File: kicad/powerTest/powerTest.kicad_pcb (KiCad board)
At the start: 2 copper layers, 34 x 30 mm, 40 parts, among them J1 Solar Panel, J10 Conn_01x01_Pin, J11 Conn_01x01_Pin, J2 BATT, J3 3V3 Sensor Bus, J4 Conn_01x01_Pin, J5 Conn_01x01_Pin, J6 Conn_01x01_Pin, J7 Conn_01x01_Pin, J8 Conn_01x01_Pin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

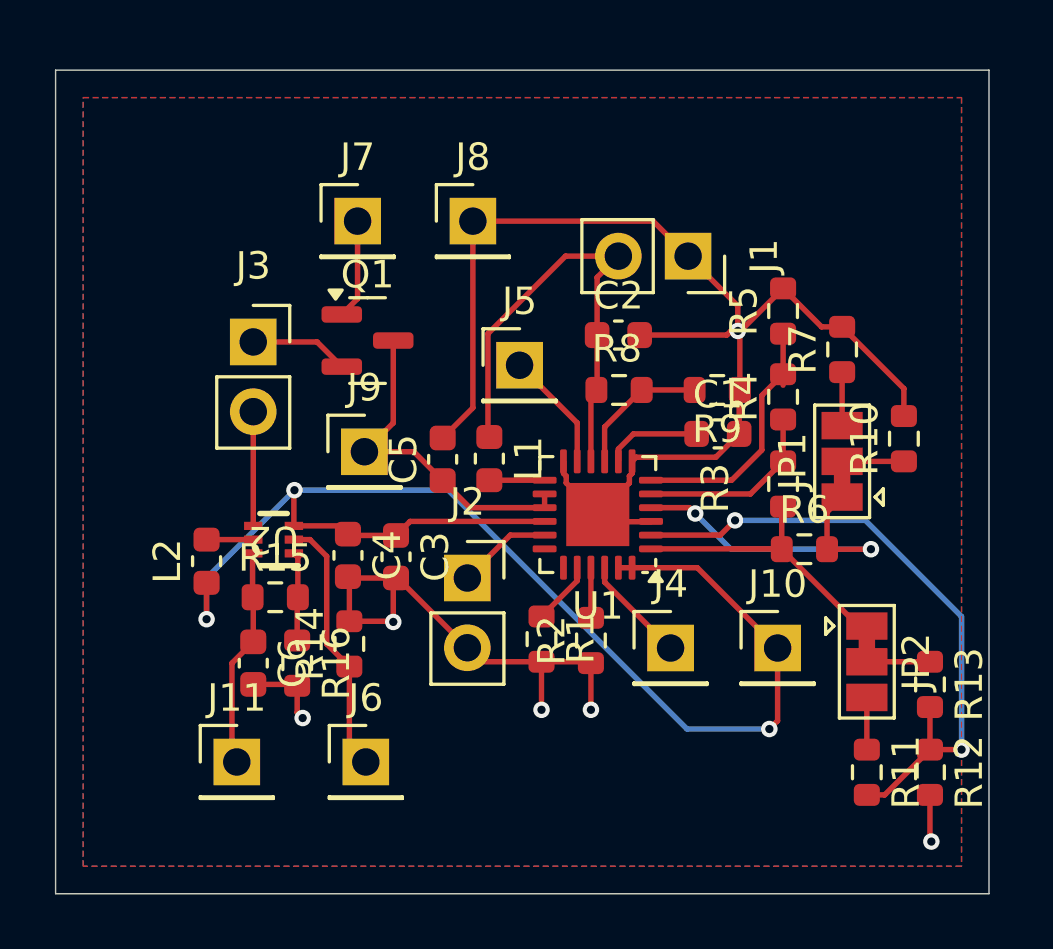
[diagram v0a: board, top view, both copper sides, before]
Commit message: Power Board Test 1.1
Updated Test Power Board
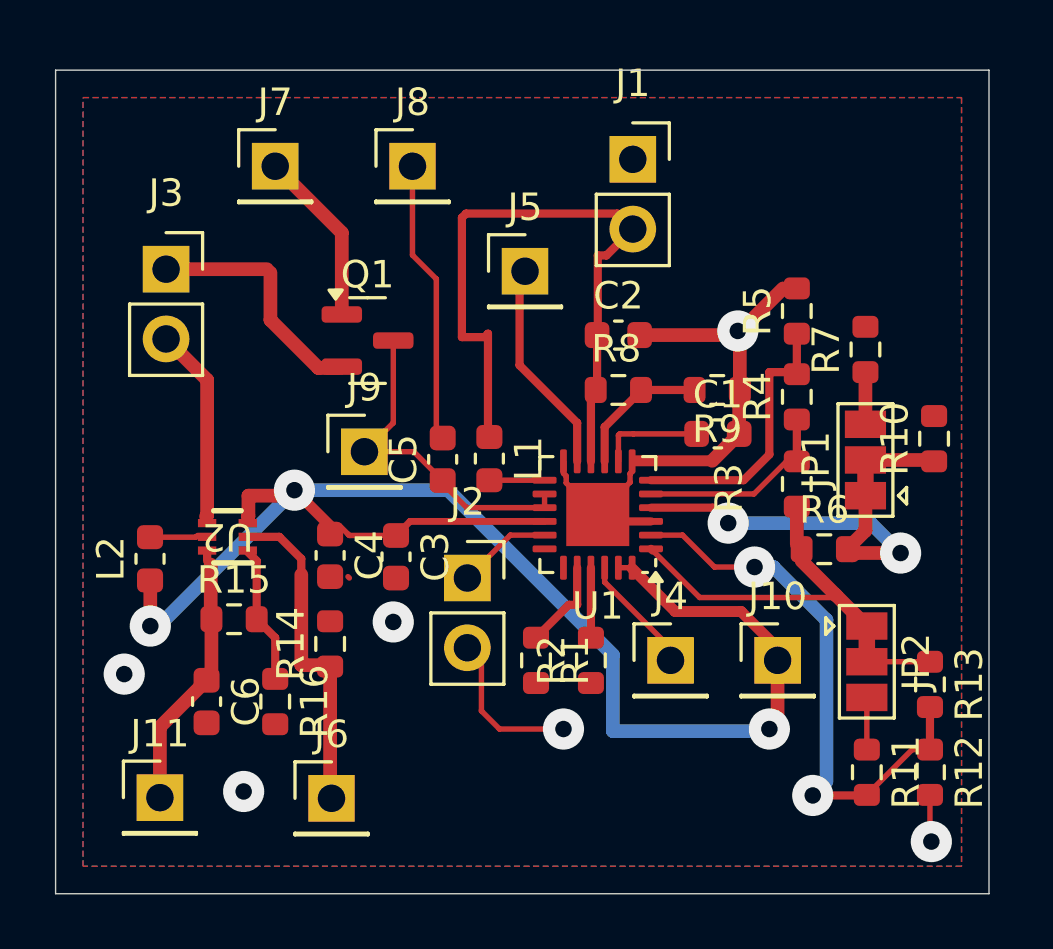
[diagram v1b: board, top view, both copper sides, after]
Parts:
- moved J3 4.14 mm to (94.0, 94.2)
- moved J1 4.06 mm to (111.0, 90.2), turned to 0 degrees
- moved J7 3.61 mm to (98.0, 90.5)
- moved J5 3.43 mm to (107.1, 94.3)
- moved J11 3.09 mm to (93.8, 113.5)
- moved J8 2.97 mm to (103.0, 90.5)
- moved C6 2.20 mm to (95.5, 110.0)
- moved L2 2.06 mm to (93.4, 104.8)
- moved J6 1.82 mm to (100.0, 113.5)
- moved R15 1.70 mm to (96.5, 107.0)
- moved U2 1.68 mm to (96.3, 104.0)
- moved R16 1.61 mm to (98.0, 110.0)
- moved R10 1.10 mm to (122.0, 100.4)
- moved JP1 0.85 mm to (119.5, 101.2)
- moved R7 0.85 mm to (119.5, 97.2)
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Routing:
- net GND: track 75.6 -> 46.8 mm
- net Net-(J1-Pin_2): track 17.6 -> 24.6 mm
- net VSS: track 49.1 -> 54.7 mm
- net Net-(J3-Pin_1): track 3.60 -> 8.92 mm
- net LLD: track 4.37 -> 7.66 mm
- net ~{SNSR_EN}: track 3.64 -> 6.40 mm
- net Net-(JP2-A): track 10.6 -> 13.3 mm
- net 5V_EN: track 9.53 -> 12.0 mm
- net /SETSD: track 23.6 -> 21.2 mm
- net +5V: track 8.01 -> 10.1 mm
- net Net-(JP1-A): track 12.4 -> 14.3 mm
- net Net-(U2-FB): track 3.25 -> 5.04 mm
- net Net-(U1-VID): track 2.31 -> 3.35 mm
- net Net-(U1-SETHYST): track 9.45 -> 10.2 mm
- net Net-(U1-MINOP): track 1.83 -> 2.55 mm
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
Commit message: updates
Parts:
- added C7: 10u, Capacitor_SMD:C_0603_1608Metric, F.Cu at (105.2, 104.7)
- added D1: 3.3V, Diode_SMD:D_0402_1005Metric_Pad0.77x0.64mm_HandSolder, F.Cu at (107.6, 90.2)
- L1: footprint Inductor_SMD:L_0603_1608Metric -> Inductor_SMD:L_Vishay_IFSC-1515AH_4x4x1.8mm
- R10: value 4.32M -> 5.1M
- R11: value 9.76M -> 10M
- R12: value 4.99M -> 4.7M
- R13: value 10.2M -> 10M
- R3: value 6.98M -> 7.5M
- R4: value 499k -> 115k
- R5: value 2.67M -> 3.3M
- R6: value 7.15M -> 7.5M
- R7: value 8.45M -> 7.5M
- R8: value 4.7M -> 5.1M
- R9: value 18M -> 20M
- moved L1 6.95 mm to (106.8, 94.3)
- moved J5 4.35 mm to (106.8, 98.7)
- moved J9 3.73 mm to (97.6, 100.2)
- moved J2 1.85 mm to (105.0, 107.3)
- moved J8 0.80 mm to (102.2, 90.5)
- moved C2 0.69 mm to (111.2, 96.7)
- moved R8 0.58 mm to (111.1, 98.7)
- moved C3 0.25 mm to (102.2, 104.7)
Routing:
- net Net-(D1-K): track 24.6 -> 15.7 mm
- net GND: track 46.8 -> 53.9 mm
- net Net-(U1-SW): track 2.01 -> 8.82 mm
- net LLD: track 7.66 -> 4.09 mm
- net +3.3V: track 12.5 -> 15.4 mm
- net Net-(J2-Pin_1): track 3.46 -> 5.20 mm
